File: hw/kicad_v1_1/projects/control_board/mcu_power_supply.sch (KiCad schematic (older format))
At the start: 11 parts, among them U5 TPS563208

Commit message: Update
Begin work on updating for rev1.1.
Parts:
- removed C20, C21: 22uF, Capacitors_ThroughHole:C_Radial_D6.3_L11.2_P2.5, symbol C
- removed C25: 0.1uF, Capacitors_SMD:C_0805_HandSoldering, symbol C
- removed L2: LBR2518T2R2M, Nixie:ind_2518, symbol LBR2518T2R2M
- removed R15, R16: 10k, Resistors_SMD:R_0805_HandSoldering, symbol R
- removed R17: 33.2k, Resistors_SMD:R_0805_HandSoldering, symbol R
- removed U5: TPS563208, Housings_SOIC:SOIC-8_3.9x4.9mm_Pitch1.27mm, symbol TPS563208
- added D?: LTST-C190GKT, LEDs:LED_0603, symbol LED-RESCUE-nixie_clock
- added R?: 330, Resistors_SMD:R_0805_HandSoldering, symbol R-RESCUE-nixie_clock
- added U?: R-78E5.0-0.5, symbol R-78E5.0-0.5
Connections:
- net labels added: +5V
- net labels removed: +3.3V
- wire segments 38 -> 21
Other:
- moved on the sheet: C22, C23, C24

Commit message: Updates to BOM
Start to update BOM for 180V supply
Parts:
- U5: renamed from U?; footprint (none) -> Nixie:R-78E5.0-0.5
- gave numbers to parts that had none: 2
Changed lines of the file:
@@
 GND
 $Comp
-L GND #PWR043
+L GND #PWR023
 U 1 1 51B54D44
 P 1750 1550
-F 0 "#PWR043" H 1750 1550 30  0001 C CNN
+F 0 "#PWR023" H 1750 1550 30  0001 C CNN
 F 1 "GND" H 1750 1480 30  0001 C CNN
 F 2 "" H 1750 1550 60  0000 C CNN
@@
 $EndComp
 $Comp
-L +12V #PWR053
+L +12V #PWR024
 U 1 1 575E2E76
 P 4450 2900
-F 0 "#PWR053" H 4450 2750 50  0001 C CNN
+F 0 "#PWR024" H 4450 2750 50  0001 C CNN
 F 1 "+12V" H 4450 3040 50  0000 C CNN
 F 2 "" H 4450 2900 50  0000 C CNN
@@
 $EndComp
 $Comp
-L +12V #PWR054
+L +12V #PWR025
 U 1 1 575E327A
 P 1750 1100
-F 0 "#PWR054" H 1750 950 50  0001 C CNN
+F 0 "#PWR025" H 1750 950 50  0001 C CNN
 F 1 "+12V" H 1750 1240 50  0000 C CNN
 F 2 "" H 1750 1100 50  0000 C CNN
@@
 $EndComp
 $Comp
-L R-78E5.0-0.5 U?
+L R-78E5.0-0.5 U5
 U 1 1 581F12A5
 P 5700 2850
-F 0 "U?" H 5700 3400 60  0000 C CNN
+F 0 "U5" H 5700 3400 60  0000 C CNN
 F 1 "R-78E5.0-0.5" H 5700 3300 60  0000 C CNN
-F 2 "" H 5700 2850 60  0000 C CNN
+F 2 "Nixie:R-78E5.0-0.5" H 5700 3500 60  0000 C CNN
 F 3 "" H 5700 2850 60  0000 C CNN
 	1    5700 2850
@@
 $EndComp
 $Comp
-L GND #PWR?
+L GND #PWR026
 U 1 1 581F154D
 P 4450 4100
-F 0 "#PWR?" H 4450 3850 50  0001 C CNN
+F 0 "#PWR026" H 4450 3850 50  0001 C CNN
 F 1 "GND" H 4450 3950 50  0000 C CNN
 F 2 "" H 4450 4100 50  0000 C CNN
@@
 $EndComp
 $Comp
-L +5V #PWR?
+L +5V #PWR027
 U 1 1 581F157B
 P 1950 1100
-F 0 "#PWR?" H 1950 950 50  0001 C CNN
+F 0 "#PWR027" H 1950 950 50  0001 C CNN
 F 1 "+5V" H 1950 1240 50  0000 C CNN
 F 2 "" H 1950 1100 50  0000 C CNN
@@
 $EndComp
 $Comp
-L +5V #PWR?
+L +5V #PWR028
 U 1 1 581F159D
 P 6900 3100
-F 0 "#PWR?" H 6900 2950 50  0001 C CNN
+F 0 "#PWR028" H 6900 2950 50  0001 C CNN
 F 1 "+5V" H 6900 3240 50  0000 C CNN
 F 2 "" H 6900 3100 50  0000 C CNN
@@
 $EndComp
 $Comp
-L GND #PWR?
+L GND #PWR029
 U 1 1 581F16C7
 P 6900 4000
-F 0 "#PWR?" H 6900 3750 50  0001 C CNN
+F 0 "#PWR029" H 6900 3750 50  0001 C CNN
 F 1 "GND" H 6900 3850 50  0000 C CNN
 F 2 "" H 6900 4000 50  0000 C CNN
@@
 $EndComp
 $Comp
-L GND #PWR?
+L GND #PWR030
 U 1 1 581F18FF
 P 5700 3600
-F 0 "#PWR?" H 5700 3350 50  0001 C CNN
+F 0 "#PWR030" H 5700 3350 50  0001 C CNN
 F 1 "GND" H 5700 3450 50  0000 C CNN
 F 2 "" H 5700 3600 50  0000 C CNN
@@
 $EndComp
 $Comp
-L R-RESCUE-nixie_clock R?
+L R-RESCUE-nixie_clock R19
 U 1 1 581F541B
 P 7950 3900
-F 0 "R?" V 8000 3700 40  0000 C CNN
+F 0 "R19" V 8000 3700 40  0000 C CNN
 F 1 "330" V 7957 3901 40  0000 C CNN
 F 2 "Resistors_SMD:R_0805_HandSoldering" V 7880 3900 30  0001 C CNN
@@
 $EndComp
 $Comp
-L LED-RESCUE-nixie_clock D?
+L LED-RESCUE-nixie_clock D7
 U 1 1 581F5422
 P 7950 4550
-F 0 "D?" H 7950 4650 50  0000 C CNN
+F 0 "D7" H 7950 4650 50  0000 C CNN
 F 1 "LTST-C190GKT" H 8150 4750 50  0000 C CNN
 F 2 "LEDs:LED_0603" H 7950 4550 60  0001 C CNN
@@
 	7950 4750 7950 4900
 $Comp
-L GND #PWR?
+L GND #PWR031
 U 1 1 581F55EB
 P 7950 4900
-F 0 "#PWR?" H 7950 4650 50  0001 C CNN
+F 0 "#PWR031" H 7950 4650 50  0001 C CNN
 F 1 "GND" H 7950 4750 50  0000 C CNN
 F 2 "" H 7950 4900 50  0000 C CNN

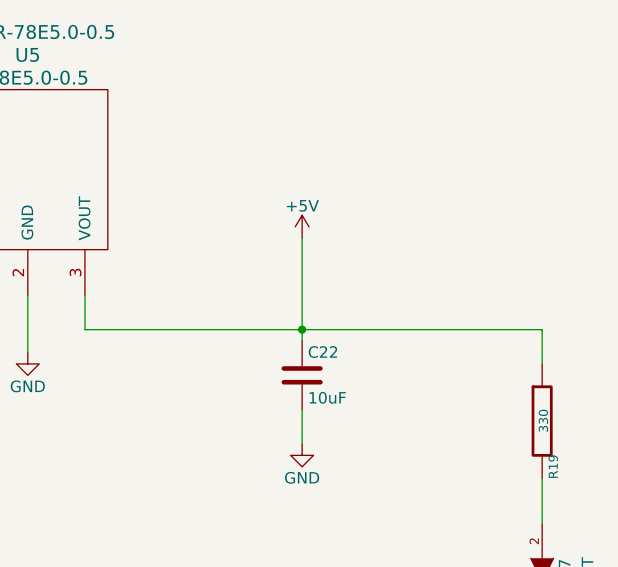
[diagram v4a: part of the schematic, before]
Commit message: Final Release
Update with trimming and bug fixes. This is what is being delivered as a
V1.1.0 release.
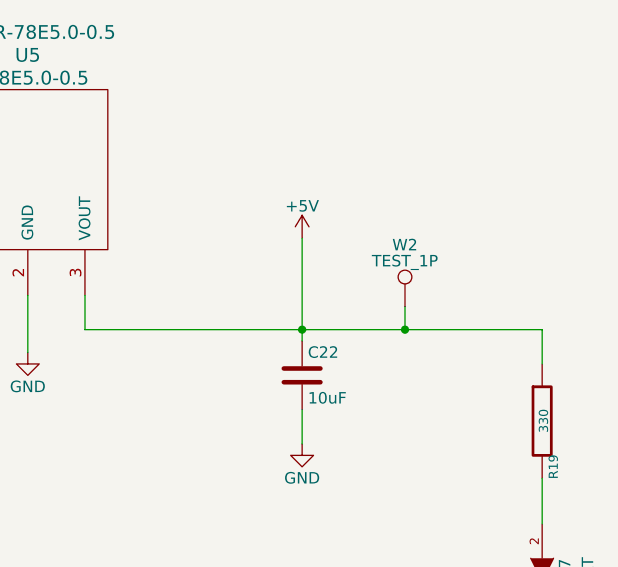
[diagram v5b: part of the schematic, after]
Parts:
- added W2: TEST_1P, Measurement_Points:Measurement_Point_Round-TH_Big, symbol TEST_1P
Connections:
- net +5V: now also W2.1
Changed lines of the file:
@@
 Sheet 3 6
 Title "Control Board"
-Date "2016-09-14"
-Rev "1.0"
+Date "2016-11-21"
+Rev "1.1"
 Comp ""
 Comment1 ""
@@
 	1    0    0    -1
 $EndComp
+$Comp
+L TEST_1P W2
+U 1 1 58353EA2
+P 7350 3400
+F 0 "W2" H 7350 3670 50  0000 C CNN
+F 1 "TEST_1P" H 7350 3600 50  0000 C CNN
+F 2 "Measurement_Points:Measurement_Point_Round-TH_Big" H 7550 3400 50  0001 C CNN
+F 3 "" H 7550 3400 50  0000 C CNN
+	1    7350 3400
+	1    0    0    -1
+$EndComp
+Wire Wire Line
+	7350 3400 7350 3500
+Connection ~ 7350 3500
 $EndSCHEMATC
